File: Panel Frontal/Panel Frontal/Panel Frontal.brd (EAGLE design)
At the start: 130 x 50 mm, 16 parts, among them J1 F0504-H-05-10G-R, Q1 BSS138, Q2 BSS138, Q3 BSS138

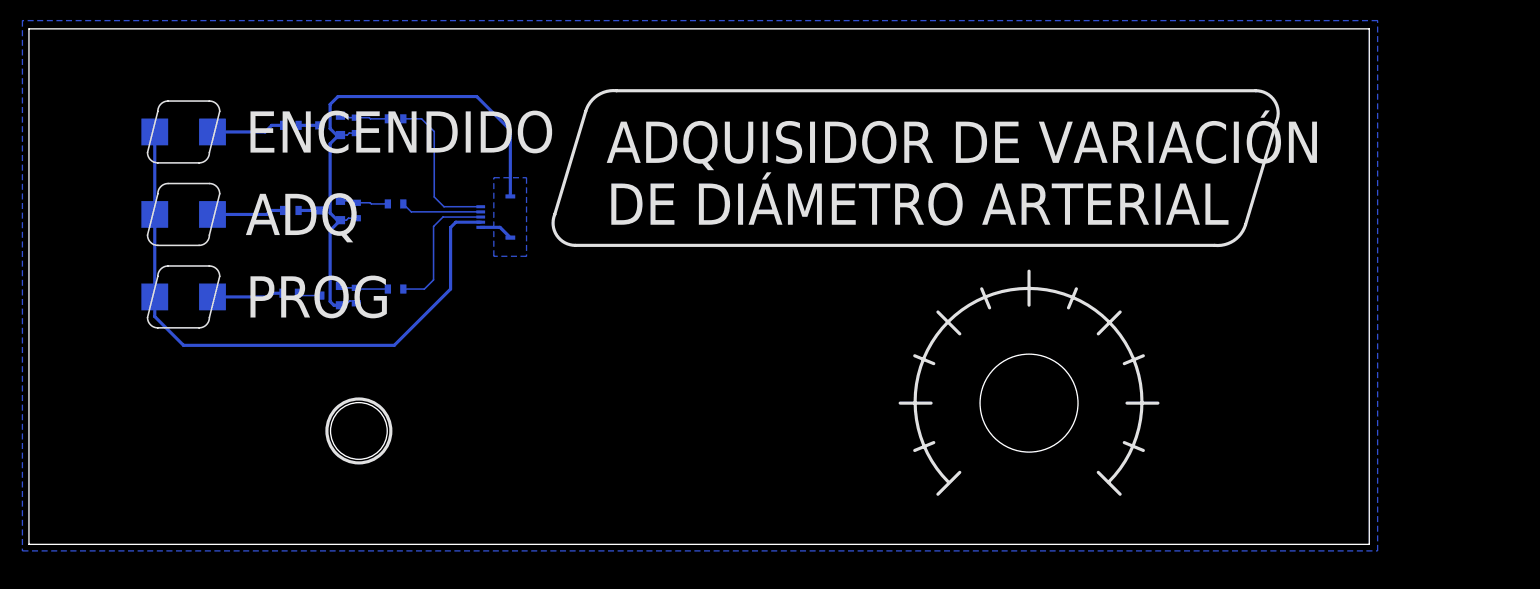
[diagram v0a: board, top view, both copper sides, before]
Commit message: trabajando en los panelizados
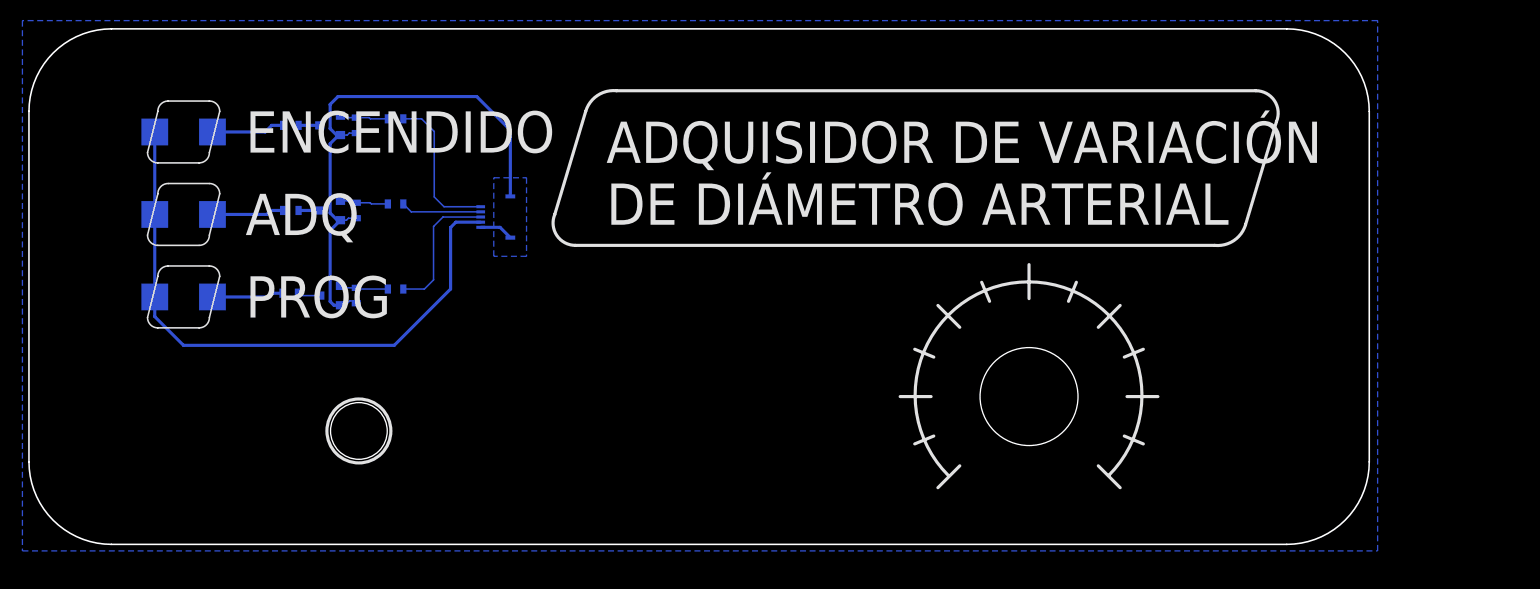
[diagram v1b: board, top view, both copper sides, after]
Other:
- outline, holes or cut-outs redrawn
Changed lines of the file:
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@@
 <setting verticaltext="up"/>
 </settings>
-<grid distance="25" unitdist="mil" unit="mil" style="lines" multiple="1" display="yes" altdistance="5" altunitdist="mil" altunit="mil"/>
+<grid distance="1" unitdist="mm" unit="mil" style="lines" multiple="1" display="yes" altdistance="5" altunitdist="mil" altunit="mil"/>
 <layers>
 <layer number="1" name="Top" color="4" fill="1" visible="yes" active="yes"/>
@@
 <layer number="14" name="Route14" color="22" fill="1" visible="no" active="no"/>
 <layer number="15" name="Route15" color="23" fill="1" visible="no" active="no"/>
-<layer number="16" name="Bottom" color="1" fill="1" visible="yes" active="yes"/>
+<layer number="16" name="Bottom" color="1" fill="1" visible="no" active="yes"/>
 <layer number="17" name="Pads" color="2" fill="1" visible="yes" active="yes"/>
 <layer number="18" name="Vias" color="2" fill="1" visible="yes" active="yes"/>
@@
 <layer number="20" name="Dimension" color="24" fill="1" visible="yes" active="yes"/>
 <layer number="21" name="tPlace" color="7" fill="1" visible="yes" active="yes"/>
-<layer number="22" name="bPlace" color="7" fill="1" visible="yes" active="yes"/>
+<layer number="22" name="bPlace" color="7" fill="1" visible="no" active="yes"/>
 <layer number="23" name="tOrigins" color="15" fill="1" visible="yes" active="yes"/>
-<layer number="24" name="bOrigins" color="15" fill="1" visible="yes" active="yes"/>
-<layer number="25" name="tNames" color="7" fill="1" visible="yes" active="yes"/>
-<layer number="26" name="bNames" color="7" fill="1" visible="yes" active="yes"/>
+<layer number="24" name="bOrigins" color="15" fill="1" visible="no" active="yes"/>
+<layer number="25" name="tNames" color="7" fill="1" visible="no" active="yes"/>
+<layer number="26" name="bNames" color="7" fill="1" visible="no" active="yes"/>
 <layer number="27" name="tValues" color="7" fill="1" visible="no" active="yes"/>
 <layer number="28" name="bValues" color="7" fill="1" visible="no" active="yes"/>
-<layer number="29" name="tStop" color="7" fill="3" visible="yes" active="yes"/>
-<layer number="30" name="bStop" color="7" fill="6" visible="yes" active="yes"/>
+<layer number="29" name="tStop" color="7" fill="3" visible="no" active="yes"/>
+<layer number="30" name="bStop" color="7" fill="6" visible="no" active="yes"/>
 <layer number="31" name="tCream" color="7" fill="4" visible="no" active="yes"/>
 <layer number="32" name="bCream" color="7" fill="5" visible="no" active="yes"/>
@@
 <layer number="37" name="tTest" color="7" fill="1" visible="no" active="yes"/>
 <layer number="38" name="bTest" color="7" fill="1" visible="no" active="yes"/>
-<layer number="39" name="tKeepout" color="4" fill="11" visible="no" active="yes"/>
+<layer number="39" name="tKeepout" color="4" fill="11" visible="yes" active="yes"/>
 <layer number="40" name="bKeepout" color="1" fill="11" visible="no" active="yes"/>
-<layer number="41" name="tRestrict" color="4" fill="10" visible="no" active="yes"/>
+<layer number="41" name="tRestrict" color="4" fill="10" visible="yes" active="yes"/>
 <layer number="42" name="bRestrict" color="1" fill="10" visible="no" active="yes"/>
 <layer number="43" name="vRestrict" color="2" fill="10" visible="no" active="yes"/>
@@
 <layer number="50" name="dxf" color="7" fill="1" visible="no" active="no"/>
 <layer number="51" name="tDocu" color="7" fill="1" visible="yes" active="yes"/>
-<layer number="52" name="bDocu" color="7" fill="1" visible="yes" active="yes"/>
+<layer number="52" name="bDocu" color="7" fill="1" visible="no" active="yes"/>
 <layer number="53" name="tGND_GNDA" color="7" fill="9" visible="no" active="no"/>
 <layer number="54" name="bGND_GNDA" color="1" fill="9" visible="no" active="no"/>
@@
 <fusionsync huburn="a.cGVyc29uYWw6dWUyZjQ5ODk2" projecturn="a.cGVyc29uYWw6dWUyZjQ5ODk2IzIwMjQxMjMwODUxNjE5OTA2" f3durn="urn:adsk.wipprod:dm.lineage:o1MHDTpaRSa_VN1bNHv2ag" pcbguid="" lastpulledtime="" lastsyncedchangeguid="" latestrevisionid="a86cdbd0-3d4a-4e67-9d85-7c0d73ba4174" lastsyncedrevisionid="a86cdbd0-3d4a-4e67-9d85-7c0d73ba4174" lastboardhashguid="9dd28874-23bc-1958-0e40-015864d9ecf1" lastpushedtime="2025-01-05T00:15:14Z" linktopcb3d="true"/>
 <plain>
-<wire x1="0" y1="0" x2="130" y2="0" width="0" layer="20"/>
-<wire x1="130" y1="0" x2="130" y2="50" width="0" layer="20"/>
-<wire x1="130" y1="50" x2="0" y2="50" width="0" layer="20"/>
-<wire x1="0" y1="50" x2="0" y2="0" width="0" layer="20"/>
 <wire x1="11.5" y1="38" x2="12.5" y2="42" width="0.1524" layer="21"/>
 <wire x1="13.5" y1="43" x2="17.5" y2="43" width="0.1524" layer="21"/>
@@
 <wire x1="54" y1="42" x2="57" y2="44" width="0.3048" layer="21" curve="-79.221362"/>
 <wire x1="54" y1="42" x2="51" y2="32" width="0.3048" layer="21"/>
-<hole x="97" y="13.7" drill="9.5"/>
-<wire x1="89.173075" y1="6.048225" x2="104.729425" y2="6.048225" width="0.3048" layer="21" curve="-270"/>
-<wire x1="88.161165625" y1="22.538834375" x2="90.2824875" y2="20.4175125" width="0.3048" layer="21"/>
-<wire x1="97" y1="26.5" x2="97" y2="23.2" width="0.3048" layer="21"/>
-<wire x1="84.5" y1="13.7" x2="87.5" y2="13.7" width="0.3048" layer="21"/>
-<wire x1="105.838834375" y1="22.538834375" x2="103.7175125" y2="20.4175125" width="0.3048" layer="21"/>
-<wire x1="109.5" y1="13.7" x2="106.5" y2="13.7" width="0.3048" layer="21"/>
-<wire x1="105.838834375" y1="4.861165625" x2="103.7175125" y2="6.9824875" width="0.3048" layer="21"/>
-<wire x1="88.161165625" y1="4.861165625" x2="90.2824875" y2="6.9824875" width="0.3048" layer="21"/>
-<wire x1="85.913446875" y1="18.2922" x2="87.76120625" y2="17.52683125" width="0.3048" layer="21"/>
-<wire x1="92.4078" y1="24.786553125" x2="93.17316875" y2="22.93879375" width="0.3048" layer="21"/>
-<wire x1="101.5922" y1="24.786553125" x2="100.82683125" y2="22.93879375" width="0.3048" layer="21"/>
-<wire x1="108.086553125" y1="18.2922" x2="106.23879375" y2="17.52683125" width="0.3048" layer="21"/>
-<wire x1="108.086553125" y1="9.1078" x2="106.23879375" y2="9.87316875" width="0.3048" layer="21"/>
-<wire x1="85.913446875" y1="9.1078" x2="87.76120625" y2="9.87316875" width="0.3048" layer="21"/>
+<hole x="97" y="14.335" drill="9.5"/>
+<wire x1="89.173075" y1="6.683225" x2="104.729425" y2="6.683225" width="0.3048" layer="21" curve="-270"/>
+<wire x1="88.161165625" y1="23.173834375" x2="90.2824875" y2="21.0525125" width="0.3048" layer="21"/>
+<wire x1="97" y1="27.135" x2="97" y2="23.835" width="0.3048" layer="21"/>
+<wire x1="84.5" y1="14.335" x2="87.5" y2="14.335" width="0.3048" layer="21"/>
+<wire x1="105.838834375" y1="23.173834375" x2="103.7175125" y2="21.0525125" width="0.3048" layer="21"/>
+<wire x1="109.5" y1="14.335" x2="106.5" y2="14.335" width="0.3048" layer="21"/>
+<wire x1="105.838834375" y1="5.496165625" x2="103.7175125" y2="7.6174875" width="0.3048" layer="21"/>
+<wire x1="88.161165625" y1="5.496165625" x2="90.2824875" y2="7.6174875" width="0.3048" layer="21"/>
+<wire x1="85.913446875" y1="18.9272" x2="87.76120625" y2="18.16183125" width="0.3048" layer="21"/>
+<wire x1="92.4078" y1="25.421553125" x2="93.17316875" y2="23.57379375" width="0.3048" layer="21"/>
+<wire x1="101.5922" y1="25.421553125" x2="100.82683125" y2="23.57379375" width="0.3048" layer="21"/>
+<wire x1="108.086553125" y1="18.9272" x2="106.23879375" y2="18.16183125" width="0.3048" layer="21"/>
+<wire x1="108.086553125" y1="9.7428" x2="106.23879375" y2="10.50816875" width="0.3048" layer="21"/>
+<wire x1="85.913446875" y1="9.7428" x2="87.76120625" y2="10.50816875" width="0.3048" layer="21"/>
 <hole x="32" y="11" drill="5.5"/>
 <circle x="32" y="11" radius="3.1" width="0.3048" layer="21"/>
@@
 </polygon>
 <text x="125.857" y="40.894" size="1.778" layer="22" rot="MR270">Diseñado por Leandro Zabala</text>
+<wire x1="8" y1="50" x2="0" y2="42" width="0.1524" layer="20" curve="90"/>
+<wire x1="0" y1="8" x2="8" y2="0" width="0.1524" layer="20" curve="90"/>
+<wire x1="130" y1="42" x2="122" y2="50" width="0.1524" layer="20" curve="90"/>
+<wire x1="122" y1="0" x2="130" y2="8" width="0.1524" layer="20" curve="90"/>
+<wire x1="130" y1="8" x2="130" y2="42" width="0.1524" layer="20"/>
+<wire x1="122" y1="50" x2="8" y2="50" width="0.1524" layer="20"/>
+<wire x1="0" y1="8" x2="0" y2="42" width="0.1524" layer="20"/>
+<wire x1="8" y1="0" x2="122" y2="0" width="0.1524" layer="20"/>
 </plain>
 <attributes>

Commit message: invertí todo el panel frontal para disminuir costo de ensamblaje
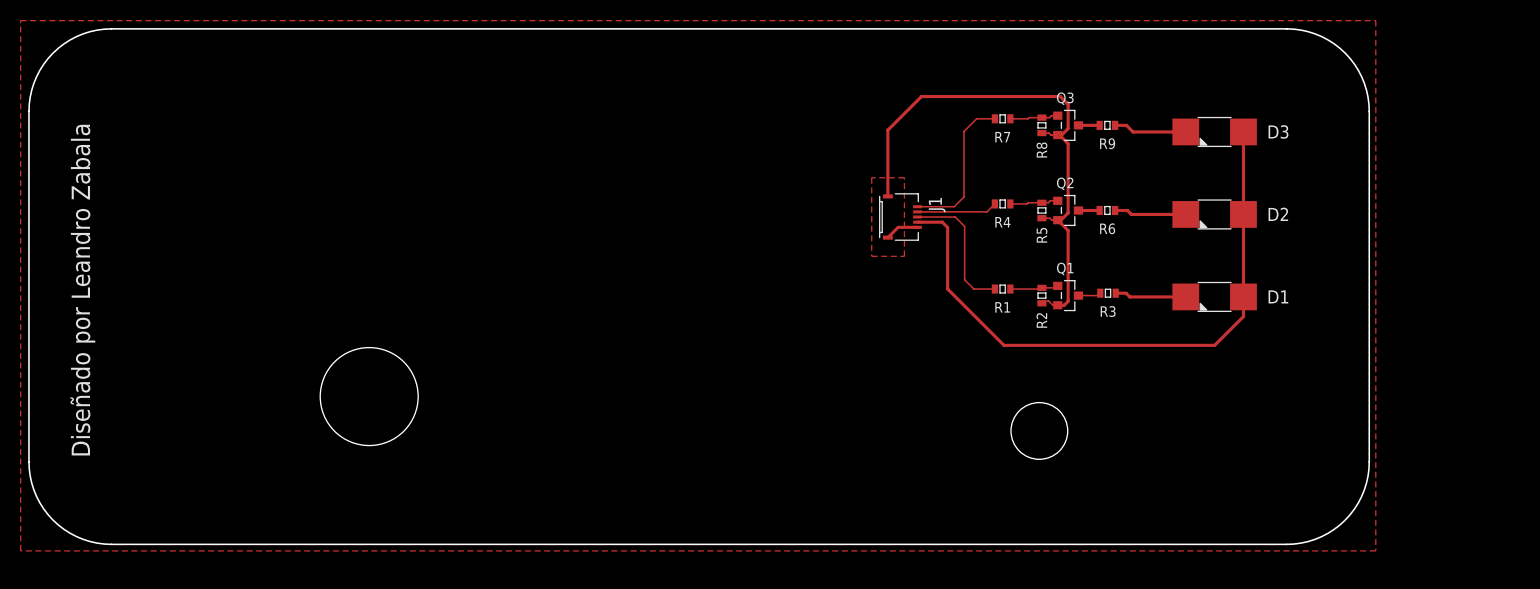
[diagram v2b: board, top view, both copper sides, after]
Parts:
- moved D1 100.0 mm to (115.0, 24.0), flipped to the top
- moved D2 100.0 mm to (115.0, 32.0), flipped to the top
- moved D3 100.0 mm to (115.0, 40.0), flipped to the top
- moved R3 79.3 mm to (104.7, 24.4), flipped to the top
- moved R6 79.2 mm to (104.6, 32.4), flipped to the top
- moved R9 79.2 mm to (104.6, 40.6), flipped to the top
- moved Q1 71.6 mm to (100.8, 24.1), flipped to the top
- moved Q2 71.6 mm to (100.8, 32.4), flipped to the top
- moved Q3 71.6 mm to (100.8, 40.6), flipped to the top
- moved R2 66.5 mm to (98.2, 24.1), flipped to the top
- moved R5 66.5 mm to (98.2, 32.4), flipped to the top
- moved R8 66.5 mm to (98.2, 40.6), flipped to the top
- moved R1 58.9 mm to (94.4, 24.8), flipped to the top
- moved R4 58.9 mm to (94.4, 33.0), flipped to the top
- moved R7 58.9 mm to (94.4, 41.3), flipped to the top
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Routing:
- added copper zone on layer 1, net GND
- removed copper zone on layer 16, net GND
